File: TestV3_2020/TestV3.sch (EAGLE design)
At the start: 57 parts, among them J3 USB_MINI-B_SMT, Q1 600mA/40V, Q2 600mA/40V, U2 MP2451

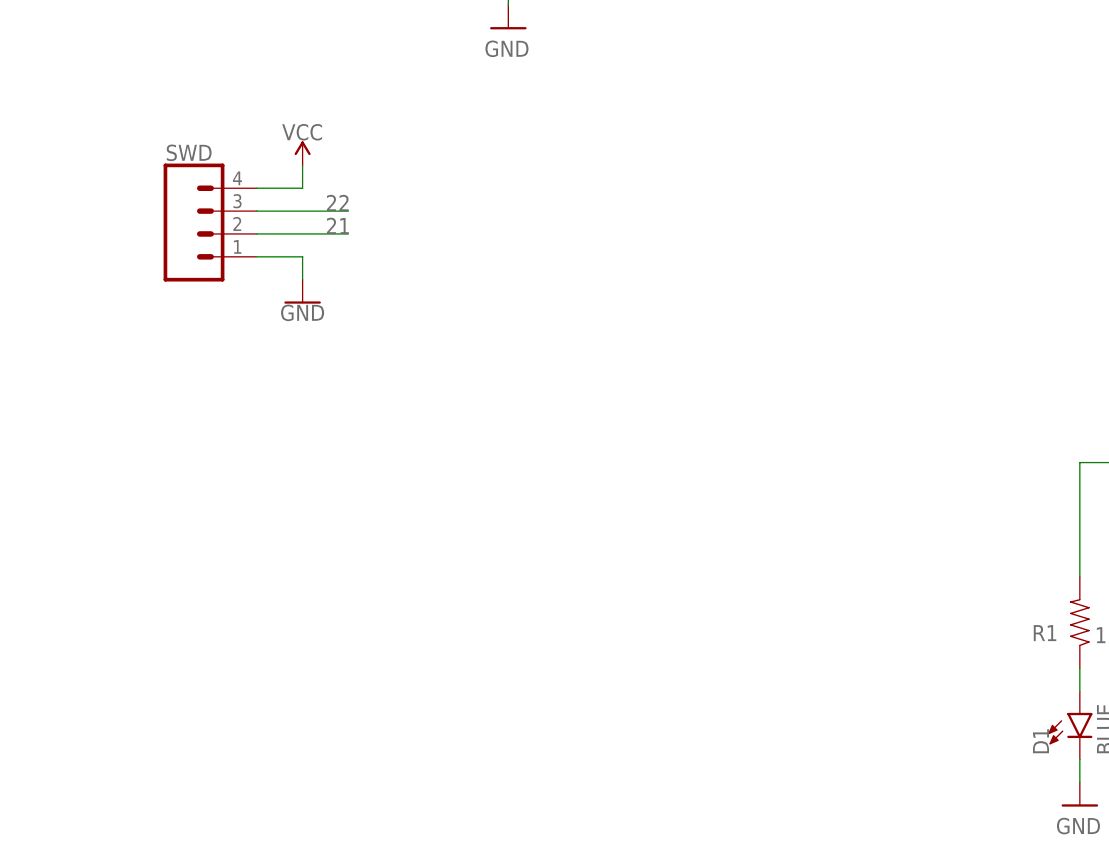
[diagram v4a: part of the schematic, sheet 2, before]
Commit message: Small changes to STM32: Added protection diodes between V_USB and VCC, and added ferrite beads to filter analog voltage
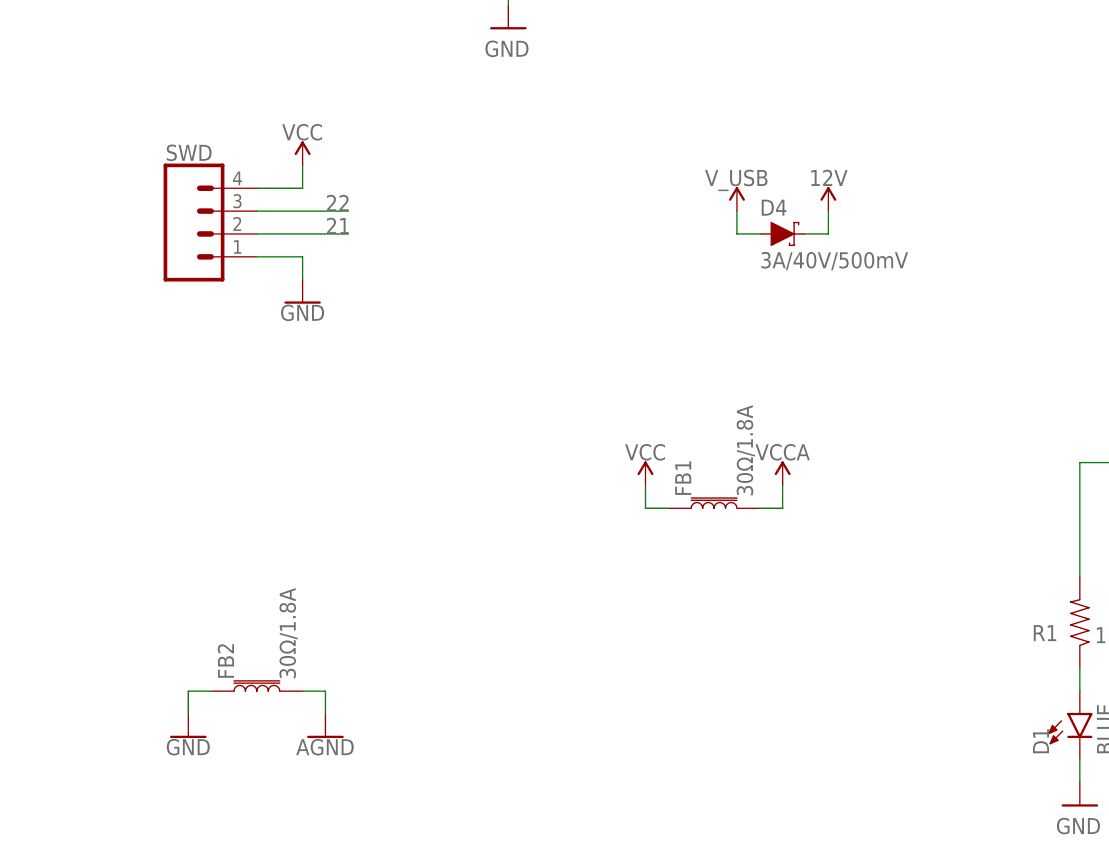
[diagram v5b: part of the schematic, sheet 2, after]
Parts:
- added D4: 3A/40V/500mV, SparkFun-DiscreteSemi:DIODE-SCHOTTKY-B340A
- added FB1, FB2: 30Ω/1.8A, SparkFun-Coils:FERRITE_BEAD-0603
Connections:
- net 12V: now also D4.C
- net AGND: now also FB2.2
- net GND: now also FB2.1
- net VCC: now also FB1.1
- net VCCA: now also FB1.2
- net V_USB: now also D4.A
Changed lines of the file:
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@@
 <drawing>
 <settings>
-<setting alwaysvectorfont="yes"/>
+<setting alwaysvectorfont="no"/>
 <setting verticaltext="up"/>
 </settings>
@@
 <part name="U$1" library="SparkFun-PowerSymbols" library_urn="urn:adsk.eagle:library:530" deviceset="AGND" device=""/>
 <part name="U$2" library="SparkFun-PowerSymbols" library_urn="urn:adsk.eagle:library:530" deviceset="AGND" device=""/>
+<part name="FB1" library="SparkFun-Coils" library_urn="urn:adsk.eagle:library:512" deviceset="FERRITE_BEAD" device="-0603" package3d_urn="urn:adsk.eagle:package:37574/1" value="30Ω/1.8A"/>
+<part name="SUPPLY9" library="SparkFun-PowerSymbols" library_urn="urn:adsk.eagle:library:530" deviceset="VCC" device=""/>
+<part name="U$4" library="SparkFun-PowerSymbols" library_urn="urn:adsk.eagle:library:530" deviceset="VCCA" device=""/>
+<part name="U$5" library="SparkFun-PowerSymbols" library_urn="urn:adsk.eagle:library:530" deviceset="AGND" device=""/>
+<part name="GND6" library="SparkFun-PowerSymbols" library_urn="urn:adsk.eagle:library:530" deviceset="GND" device=""/>
+<part name="FB2" library="SparkFun-Coils" library_urn="urn:adsk.eagle:library:512" deviceset="FERRITE_BEAD" device="-0603" package3d_urn="urn:adsk.eagle:package:37574/1" value="30Ω/1.8A"/>
+<part name="SUPPLY15" library="SparkFun-PowerSymbols" library_urn="urn:adsk.eagle:library:530" deviceset="V_USB" device=""/>
+<part name="SUPPLY18" library="SparkFun-PowerSymbols" library_urn="urn:adsk.eagle:library:530" deviceset="12V" device=""/>
+<part name="D4" library="SparkFun-DiscreteSemi" library_urn="urn:adsk.eagle:library:514" deviceset="DIODE-SCHOTTKY" device="-B340A" package3d_urn="urn:adsk.eagle:package:38443/1" value="3A/40V/500mV"/>
 </parts>
 <sheets>
@@
 <instance part="U$2" gate="G$1" x="162.56" y="124.46" smashed="yes">
 <attribute name="VALUE" x="162.56" y="124.206" size="1.778" layer="96" align="top-center"/>
+</instance>
+<instance part="FB1" gate="G$1" x="83.82" y="60.96" smashed="yes" rot="R90">
+<attribute name="NAME" x="81.28" y="62.23" size="1.778" layer="95" font="vector" rot="R90"/>
+<attribute name="VALUE" x="86.36" y="62.23" size="1.778" layer="96" font="vector" rot="R90" align="top-left"/>
+</instance>
+<instance part="SUPPLY9" gate="G$1" x="76.2" y="63.5" smashed="yes">
+<attribute name="VALUE" x="76.2" y="66.294" size="1.778" layer="96" align="bottom-center"/>
+</instance>
+<instance part="U$4" gate="G$1" x="91.44" y="63.5" smashed="yes">
+<attribute name="VALUE" x="91.44" y="66.294" size="1.778" layer="96" align="bottom-center"/>
+</instance>
+<instance part="U$5" gate="G$1" x="40.64" y="35.56" smashed="yes">
+<attribute name="VALUE" x="40.64" y="35.306" size="1.778" layer="96" align="top-center"/>
+</instance>
+<instance part="GND6" gate="1" x="25.4" y="35.56" smashed="yes">
+<attribute name="VALUE" x="25.4" y="35.306" size="1.778" layer="96" align="top-center"/>
+</instance>
+<instance part="FB2" gate="G$1" x="33.02" y="40.64" smashed="yes" rot="R90">
+<attribute name="NAME" x="30.48" y="41.91" size="1.778" layer="95" font="vector" rot="R90"/>
+<attribute name="VALUE" x="35.56" y="41.91" size="1.778" layer="96" font="vector" rot="R90" align="top-left"/>
+</instance>
+<instance part="SUPPLY15" gate="G$1" x="86.36" y="93.98" smashed="yes">
+<attribute name="VALUE" x="86.36" y="96.774" size="1.778" layer="96" align="bottom-center"/>
+</instance>
+<instance part="SUPPLY18" gate="G$1" x="96.52" y="93.98" smashed="yes">
+<attribute name="VALUE" x="96.52" y="96.774" size="1.778" layer="96" align="bottom-center"/>
+</instance>
+<instance part="D4" gate="G$1" x="91.44" y="91.44" smashed="yes">
+<attribute name="NAME" x="88.9" y="93.472" size="1.778" layer="95" font="vector"/>
+<attribute name="VALUE" x="88.9" y="89.408" size="1.778" layer="96" font="vector" align="top-left"/>
 </instance>
 </instances>
@@
 <wire x1="38.1" y1="99.06" x2="38.1" y2="96.52" width="0.1524" layer="91"/>
 </segment>
+<segment>
+<pinref part="FB1" gate="G$1" pin="1"/>
+<wire x1="78.74" y1="60.96" x2="76.2" y2="60.96" width="0.1524" layer="91"/>
+<pinref part="SUPPLY9" gate="G$1" pin="VCC"/>
+<wire x1="76.2" y1="60.96" x2="76.2" y2="63.5" width="0.1524" layer="91"/>
+</segment>
 </net>
 <net name="N$51" class="0">
@@
 <wire x1="38.1" y1="88.9" x2="38.1" y2="86.36" width="0.1524" layer="91"/>
 <pinref part="GND5" gate="1" pin="GND"/>
+</segment>
+<segment>
+<pinref part="FB2" gate="G$1" pin="1"/>
+<wire x1="27.94" y1="40.64" x2="25.4" y2="40.64" width="0.1524" layer="91"/>
+<pinref part="GND6" gate="1" pin="GND"/>
+<wire x1="25.4" y1="40.64" x2="25.4" y2="38.1" width="0.1524" layer="91"/>
 </segment>
 </net>
@@
 <pinref part="U$3" gate="G$1" pin="VCCA"/>
 </segment>
+<segment>
+<pinref part="FB1" gate="G$1" pin="2"/>
+<wire x1="88.9" y1="60.96" x2="91.44" y2="60.96" width="0.1524" layer="91"/>
+<pinref part="U$4" gate="G$1" pin="VCCA"/>
+<wire x1="91.44" y1="60.96" x2="91.44" y2="63.5" width="0.1524" layer="91"/>
+</segment>
 </net>
 <net name="V_USB" class="0">
@@
 <pinref part="SUPPLY16" gate="G$1" pin="V_USB"/>
 </segment>
+<segment>
+<pinref part="SUPPLY15" gate="G$1" pin="V_USB"/>
+<wire x1="86.36" y1="91.44" x2="86.36" y2="93.98" width="0.1524" layer="91"/>
+<pinref part="D4" gate="G$1" pin="A"/>
+<wire x1="86.36" y1="91.44" x2="88.9" y2="91.44" width="0.1524" layer="91"/>
+</segment>
 </net>
 <net name="AGND" class="0">
@@
 <pinref part="U$2" gate="G$1" pin="AGND"/>
 </segment>
-</net>
+<segment>
+<pinref part="FB2" gate="G$1" pin="2"/>
+<wire x1="38.1" y1="40.64" x2="40.64" y2="40.64" width="0.1524" layer="91"/>
+<pinref part="U$5" gate="G$1" pin="AGND"/>
+<wire x1="40.64" y1="40.64" x2="40.64" y2="38.1" width="0.1524" layer="91"/>
+</segment>
+</net>
+<net name="12V" class="0">
+<segment>
+<pinref part="D4" gate="G$1" pin="C"/>
+<wire x1="93.98" y1="91.44" x2="96.52" y2="91.44" width="0.1524" layer="91"/>
+<pinref part="SUPPLY18" gate="G$1" pin="12V"/>
+<wire x1="96.52" y1="91.44" x2="96.52" y2="93.98" width="0.1524" layer="91"/>
+</segment>
+</net>

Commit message: IDK what I did but added datasheet of INA20x current shunt controller cuz will be using that
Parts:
- added U3: LM2587, JH:LM2587
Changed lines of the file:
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@@
 <drawing>
 <settings>
-<setting alwaysvectorfont="no"/>
+<setting alwaysvectorfont="yes"/>
 <setting verticaltext="up"/>
 </settings>
@@
 </classes>
 <parts>
-<part name="FRAME1" library="SparkFun-Aesthetics" deviceset="FRAME-A4L" device=""/>
+<part name="FRAME1" library="SparkFun-Aesthetics" library_urn="urn:adsk.eagle:library:507" deviceset="FRAME-A4L" device=""/>
 <part name="C10" library="JH" library_urn="urn:adsk.eagle:library:6027132" deviceset="CAPACITOR" device="0603" package3d_urn="urn:adsk.eagle:package:15441226/3" value="47pF"/>
 <part name="C11" library="JH" library_urn="urn:adsk.eagle:library:6027132" deviceset="CAPACITOR" device="0603" package3d_urn="urn:adsk.eagle:package:15441226/3" value="47pF"/>
@@
 <part name="SUPPLY17" library="SparkFun-PowerSymbols" library_urn="urn:adsk.eagle:library:530" deviceset="GND" device="" value="GND"/>
 <part name="OSC" library="SparkFun-Clocks" library_urn="urn:adsk.eagle:library:511" deviceset="CRYSTAL" device="SMD-5X3.2-2PAD" package3d_urn="urn:adsk.eagle:package:37520/1" value="8MHz"/>
-<part name="FRAME2" library="SparkFun-Aesthetics" deviceset="FRAME-A4L" device=""/>
+<part name="FRAME2" library="SparkFun-Aesthetics" library_urn="urn:adsk.eagle:library:507" deviceset="FRAME-A4L" device=""/>
 <part name="J3" library="SparkFun-Connectors" library_urn="urn:adsk.eagle:library:513" deviceset="USB_MINI-B" device="_SMT" package3d_urn="urn:adsk.eagle:package:38244/1"/>
 <part name="U$3" library="SparkFun-PowerSymbols" library_urn="urn:adsk.eagle:library:530" deviceset="VCCA" device=""/>
 <part name="SUPPLY8" library="SparkFun-PowerSymbols" library_urn="urn:adsk.eagle:library:530" deviceset="V_USB" device=""/>
 <part name="SUPPLY16" library="SparkFun-PowerSymbols" library_urn="urn:adsk.eagle:library:530" deviceset="V_USB" device=""/>
-<part name="FRAME3" library="SparkFun-Aesthetics" deviceset="FRAME-A4L" device=""/>
+<part name="FRAME3" library="SparkFun-Aesthetics" library_urn="urn:adsk.eagle:library:507" deviceset="FRAME-A4L" device=""/>
 <part name="U2" library="JH" library_urn="urn:adsk.eagle:library:6027132" deviceset="MP245X" device="" package3d_urn="urn:adsk.eagle:package:15213528/2" value="MP2451"/>
 <part name="2R1" library="JH" library_urn="urn:adsk.eagle:library:6027132" deviceset="RESISTOR" device="0603" package3d_urn="urn:adsk.eagle:package:15441228/3" value="124k"/>
@@
 <part name="SUPPLY18" library="SparkFun-PowerSymbols" library_urn="urn:adsk.eagle:library:530" deviceset="12V" device=""/>
 <part name="D4" library="SparkFun-DiscreteSemi" library_urn="urn:adsk.eagle:library:514" deviceset="DIODE-SCHOTTKY" device="-B340A" package3d_urn="urn:adsk.eagle:package:38443/1" value="3A/40V/500mV"/>
+<part name="FRAME4" library="SparkFun-Aesthetics" library_urn="urn:adsk.eagle:library:507" deviceset="FRAME-A4L" device=""/>
+<part name="U3" library="JH" library_urn="urn:adsk.eagle:library:6027132" deviceset="LM2587" device="" package3d_urn="urn:adsk.eagle:package:9157861/2"/>
 </parts>
 <sheets>
@@
 <attribute name="LAST_DATE_TIME" x="186.69" y="11.43" size="2.286" layer="94" font="vector"/>
 <attribute name="SHEET" x="200.66" y="6.35" size="2.54" layer="94" font="vector"/>
-<attribute name="DESIGNER" x="231.34" y="11.43" size="2.54" layer="94" font="vector"/>
 </instance>
 <instance part="J3" gate="G$1" x="25.4" y="132.08" smashed="yes" rot="MR0">
@@
 <attribute name="LAST_DATE_TIME" x="186.69" y="11.43" size="2.286" layer="94" font="vector"/>
 <attribute name="SHEET" x="200.66" y="6.35" size="2.54" layer="94" font="vector"/>
-<attribute name="DESIGNER" x="231.34" y="11.43" size="2.54" layer="94" font="vector"/>
 </instance>
 <instance part="U2" gate="U1" x="193.04" y="154.94" smashed="yes">
@@
 </nets>
 </sheet>
+<sheet>
+<description>Boost Circuits</description>
+<plain>
+</plain>
+<instances>
+<instance part="FRAME4" gate="G$1" x="5.08" y="5.08" smashed="yes">
+<attribute name="DRAWING_NAME" x="186.69" y="16.51" size="2.54" layer="94" font="vector"/>
+<attribute name="LAST_DATE_TIME" x="186.69" y="11.43" size="2.286" layer="94" font="vector"/>
+<attribute name="SHEET" x="200.66" y="6.35" size="2.54" layer="94" font="vector"/>
+</instance>
+<instance part="U3" gate="G$1" x="106.68" y="121.92" smashed="yes">
+<attribute name="NAME" x="106.68" y="128.524" size="1.397" layer="95" font="vector" ratio="12" align="center"/>
+</instance>
+</instances>
+<busses>
+</busses>
+<nets>
+</nets>
+</sheet>

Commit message: Finally finished LM2587 Boost Circuit, together with INA169+LM393 overcurrent protection
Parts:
- added 3C1: 100uF, SparkFun-Capacitors:100UF-POLAR-25V-20%(ELEC)
- added 3C2, C12: 1uF, JH:CAPACITOR0603
- added 3C3, 3C5: 0.1uF, JH:CAPACITOR0603
- added 3C4: 1000uF, JH:1000UF-CAP
- added 3D1: SS510, diode:SCHOTTKY-DIODESMD
- added 3L1: 56uH, JH:INDUCTORCDRH127
- added 3R1: 2.94k, JH:RESISTOR0603
- added 3R2: 1.5k, JH:RESISTOR0603
- added 3U1: LM2587, JH:LM2587
- added C3: 100uF, SparkFun-Capacitors:100UF-POLAR-10X10.5-63V-20%
- added D5: SS34, SparkFun-DiscreteSemi:DIODE-SCHOTTKY-SS14
- added J1: (no value), SparkFun-Connectors:CONN_03LOCK
- added POT1, POT2: 10k, JH:3296-TRIMPOT
- added R18: 45k, JH:RESISTOR0603
- added R19: 0.15, SparkFun-Resistors:RESISTOR0805
- added R20: 3k, JH:RESISTOR0603
- added R21: 10k, JH:RESISTOR0603
- added U$6: LM393, JH:LM393
- added U4: INA169, SparkFun-IC-Special-Function:INA169
- J3: value USB_MINI-B_SMT -> (none); device SparkFun-Connectors:USB_MINI-B_SMT -> SparkFun-Connectors:USB_MICRO-B_FEMALE-SMT
- U3: value LM2587 -> 10k; device JH:LM2587 -> JH:MCP41XXX
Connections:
- new net FDBK: 3R2.2, 3U1.FDBK, D5.C, POT1.CCW, POT1.WIPER
- new net N$14: 3C4.+, 3D1.C, C3.+, R18.2, R19.1, U4.VIN+
- new net N$16: POT1.CW, U3POT1.CCW, U3POT1.WIPER
- new net N$17: R21.2, U$6G$2.+IN, U4.OUT
- new net N$18: R18.1, U3POT1.CW
- new net N$19: D5.A, R20.1, U$6G$2.OUT
- new net N$20: POT2.WIPER, U$6G$2.-IN
- new net N$22: J1.1, U3U1.MOSI
- new net N$23: J1.2, U3U1.SCLK
- new net N$24: J1.3, U3U1.CS
- new net N$34: 3D1.A, 3L1.2, 3U1.SW
- new net N$36: 3R1.2, 3U1.COMP
- new net N$37: 3C2.1, 3R1.1
- new net VCC_2: R19.2, U4.VIN-
- net 12V: now also 3C1.+, 3C5.1, 3L1.1, 3U1.VIN, U4.V+
- net 3.3V: now also 3C3.1, C12.1, POT2.CCW, R20.2, U$6G$1.P$V+, U3U1.VCC
- net GND: now also 3C1.-, 3C2.2, 3C3.2, 3C4.-, 3C5.2, 3R2.1, 3U1.GND, C12.2, C3.-, POT2.CW, R21.1, U$6G$1.P$V-, U3U1.GND, U4.GND

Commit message: Finished low battery detection, motor driver and TCS3200 color sensor.
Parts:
- added C13: 2.2uF/6.3V, JH:CAPACITOR0603
- added C14: 10nF/16V, JH:CAPACITOR0603
- added C15, C16: 10uF/16V, JH:CAPACITOR0805
- added C17, C18: 1uF, JH:CAPACITOR0603
- added C19: 4.7uF, JH:CAPACITOR0603
- added C20: 0.1uF, JH:CAPACITOR0603
- added CS1: TCS3200, JH:TCS3200
- added D6: BLUE, SparkFun-LED:LED-BLUE0603
- added Q3, Q4: 600mA/40V, SparkFun-DiscreteSemi:TRANS_NPN-MMBT2222AL
- added R22: 3.6k, JH:RESISTOR0603
- added R23: 75k, JH:RESISTOR0603
- added R24, R29: 100k, JH:RESISTOR0603
- added R25: 560, JH:RESISTOR0603
- added R26, R27: 0.2, JH:RESISTOR0603
- added R28: 20k-75k, JH:RESISTOR0603
- added R30: 10k, JH:RESISTOR0603
- added U5: (no value), JH:DRV8833
- added U6: (no value), SparkFun-IC-Power:V_REG_LM1117SOT223
- 2C11, 2C12: value 47uF -> 47uF/6.3v
- D4: value 3A/40V/500mV -> SS34
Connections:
- new net N$21: Q3.C, Q4.B, R24.1
- new net N$25: D6.A, R25.2
- new net N$26: D6.C, Q4.C
- new net N$27: U5.A-IN1
- new net N$28: Q3.B, R22.2, R23.1
- new net N$29: U5.A-IN2
- new net N$30: U5.B-IN1
- new net N$31: U5.B-IN2
- new net N$32: R28.1, U5.SLEEP
- new net N$33: R29.1, U5.FAULT
- new net N$35: R26.2, U5.B-ISEN
- new net N$38: R27.2, U5.A-ISEN
- new net N$39: U5.A-OUT1
- new net N$40: U5.A-OUT2
- new net N$41: U5.B-OUT1
- new net N$42: U5.B-OUT2
- new net N$43: C14.1, U5.VCP
- new net N$44: C13.1, U5.VINT
- new net N$45: CS1.S0
- new net N$46: CS1.S1
- new net N$47: CS1.S2
- new net N$48: CS1.S3
- new net N$49: CS1.OUT
- new net N$50: CS1.OE, R30.2
- new net VCC_1: C14.2, C15.1, C16.1, R28.2, R29.2, U5.VM
- net 12V: now also C19.1, R23.2, R24.2, R25.1, U6.IN
- net 3.3V: now also C20.2, CS1.VIN
- net AGND: now also C18.2
- net GND: now also C13.2, C15.2, C16.2, C17.2, C19.2, C20.1, CS1.GND, Q3.E, Q4.E, R22.1, R26.1, R27.1, R30.1, U5.GND, U6.ADJ
- net VCC: now also C17.1, U6.OUT, U6.OUT@1
- net VCCA: now also C18.1
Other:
- note added: "MAX 10v!!"
- note added: "PWM Pins!!"
- note added: "use xh2.54 here"
